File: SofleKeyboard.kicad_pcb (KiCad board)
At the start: 2 copper layers, 82 parts, among them J3 OLED, SW1 SW_PUSH_LED, SW10 SW_PUSH_LED, SW11 SW_PUSH_LED, SW12 SW_PUSH_LED, SW13 SW_PUSH_LED, SW14 SW_PUSH_LED, SW15 SW_PUSH_LED, SW16 SW_PUSH_LED, SW17 SW_PUSH_LED, SW18 SW_PUSH_LED, SW19 SW_PUSH_LED, SW2 SW_PUSH_LED, SW20 SW_PUSH_LED, SW21 SW_PUSH_LED, SW22 SW_PUSH_LED, SW23 SW_PUSH_LED, SW24 SW_PUSH_LED, SW26 SW_PUSH_LED, SW27 SW_PUSH_LED, SW28 SW_PUSH_LED, SW29 SW_PUSH_LED, SW3 SW_PUSH_LED, SW30 SW_PUSH_LED, SW4 SW_PUSH_LED, SW5 SW_PUSH_LED, SW6 SW_PUSH_LED, SW7 SW_PUSH_LED, SW8 SW_PUSH_LED, SW9 SW_PUSH_LED, U1 ProMicro

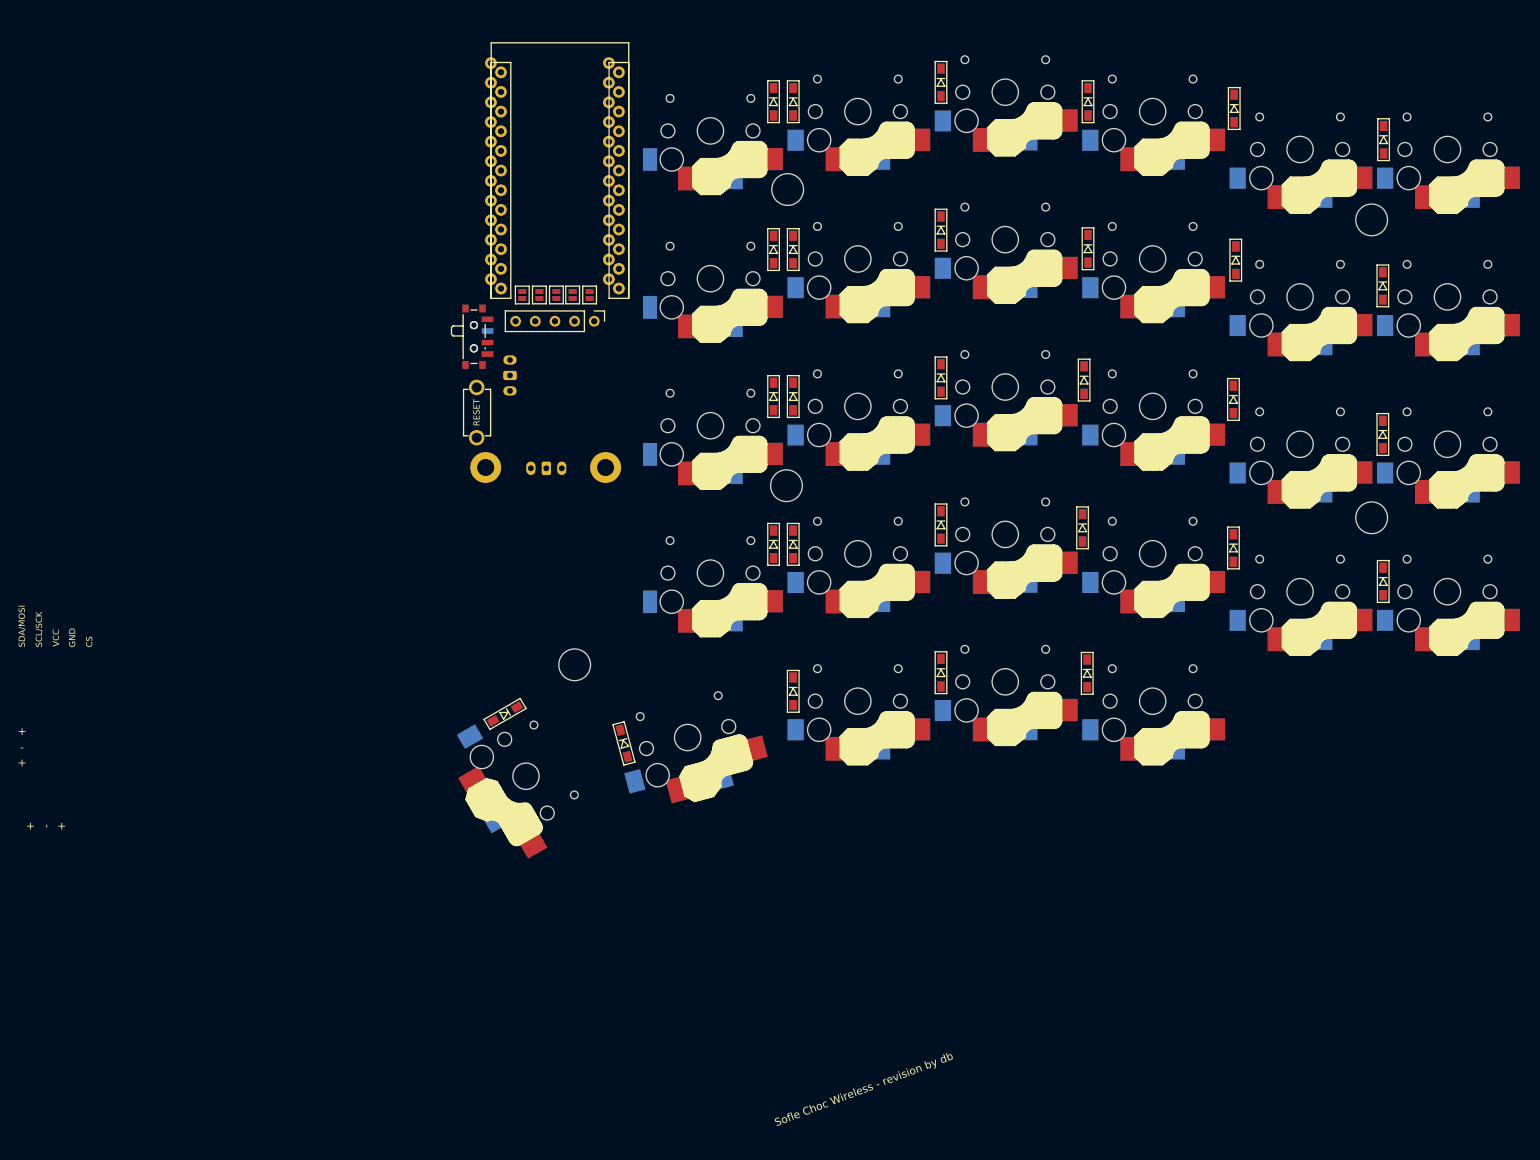
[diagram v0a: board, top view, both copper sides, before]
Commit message: add sofle library, pcb outline, link new footprints to pcb
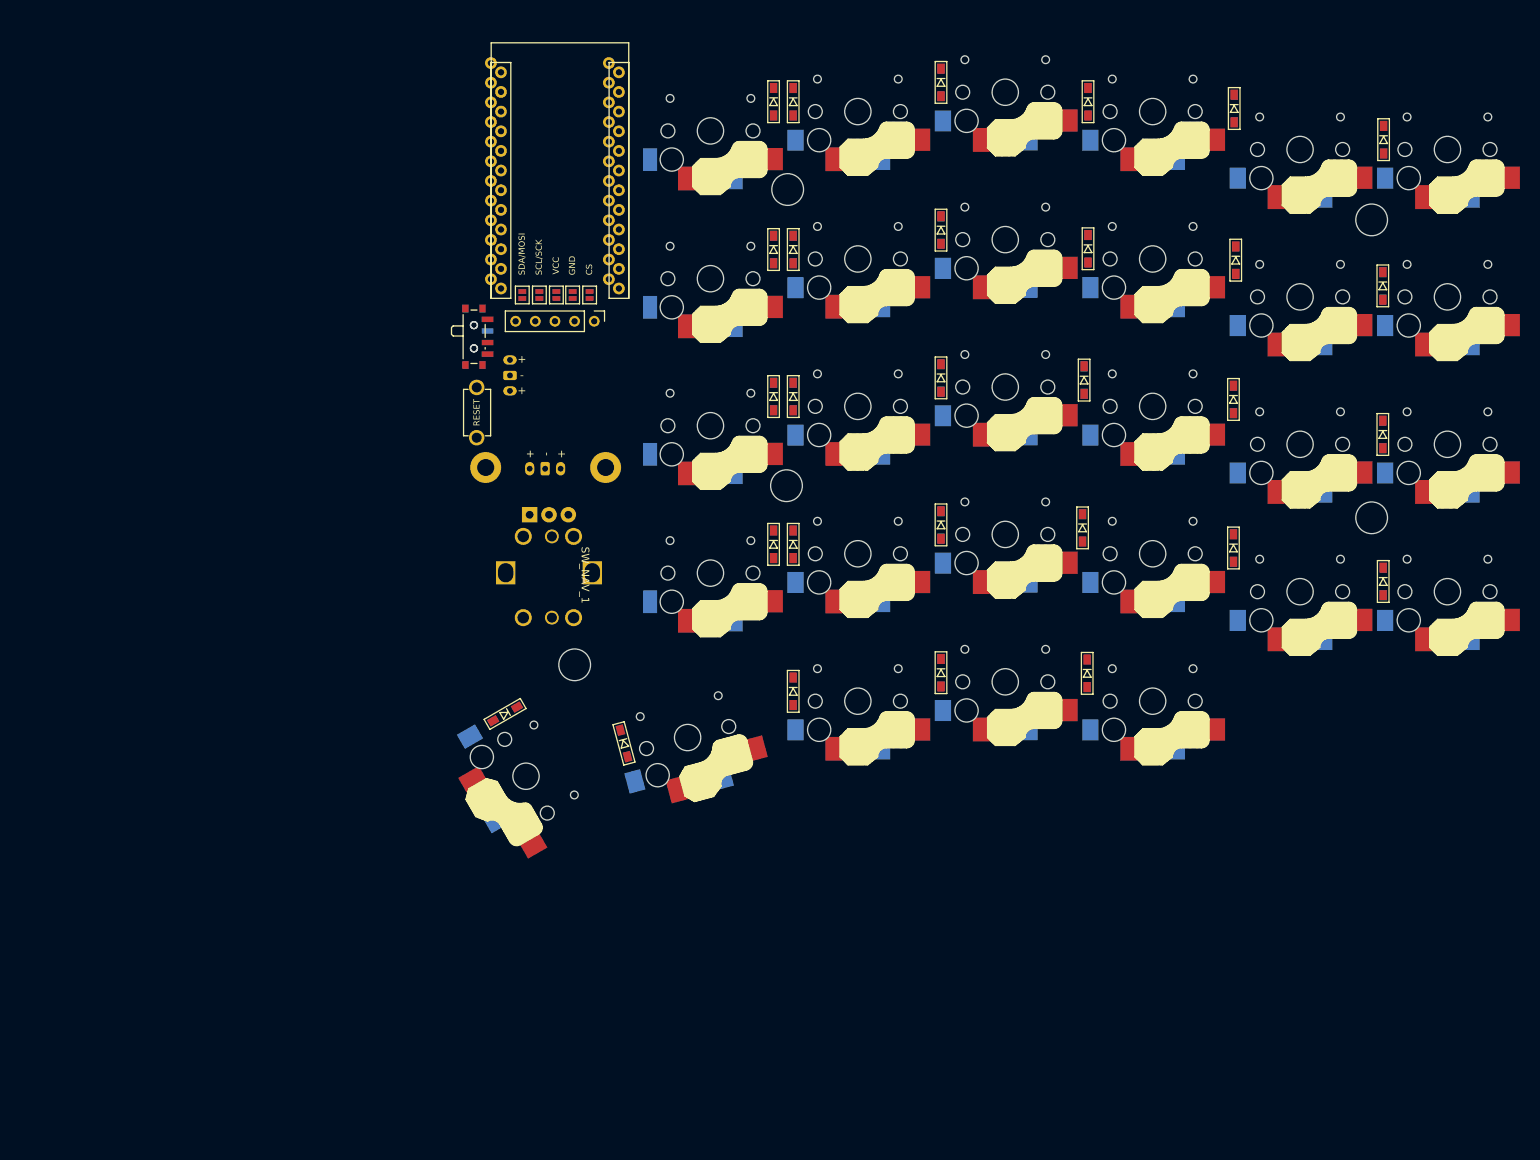
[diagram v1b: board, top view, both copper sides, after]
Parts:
- added ENC1: RotaryEncoder, Rotary_Encoder:RotaryEncoder_Alps_EC12E_Vertical_H20mm, B.Cu at (161.8, 51.6)
- added SW_NAV_1: SW_NAV, VicoKeyboard:NavSwitch_5Way, F.Cu at (168.5, 59.4)
- moved JST_BATT1 0.16 mm to (163.8, 45.7)
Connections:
- U1 pad 2: LED -> unconnected-(U1-RX(PD2)-Pad2)
- U1 pad 7: unconnected-(U1-Pad7) -> col6
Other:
- board text removed: "Sofle Choc Wireless - revision by db"
- board text removed: "s25"

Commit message: jlc rules, add board outline in edge.cuts
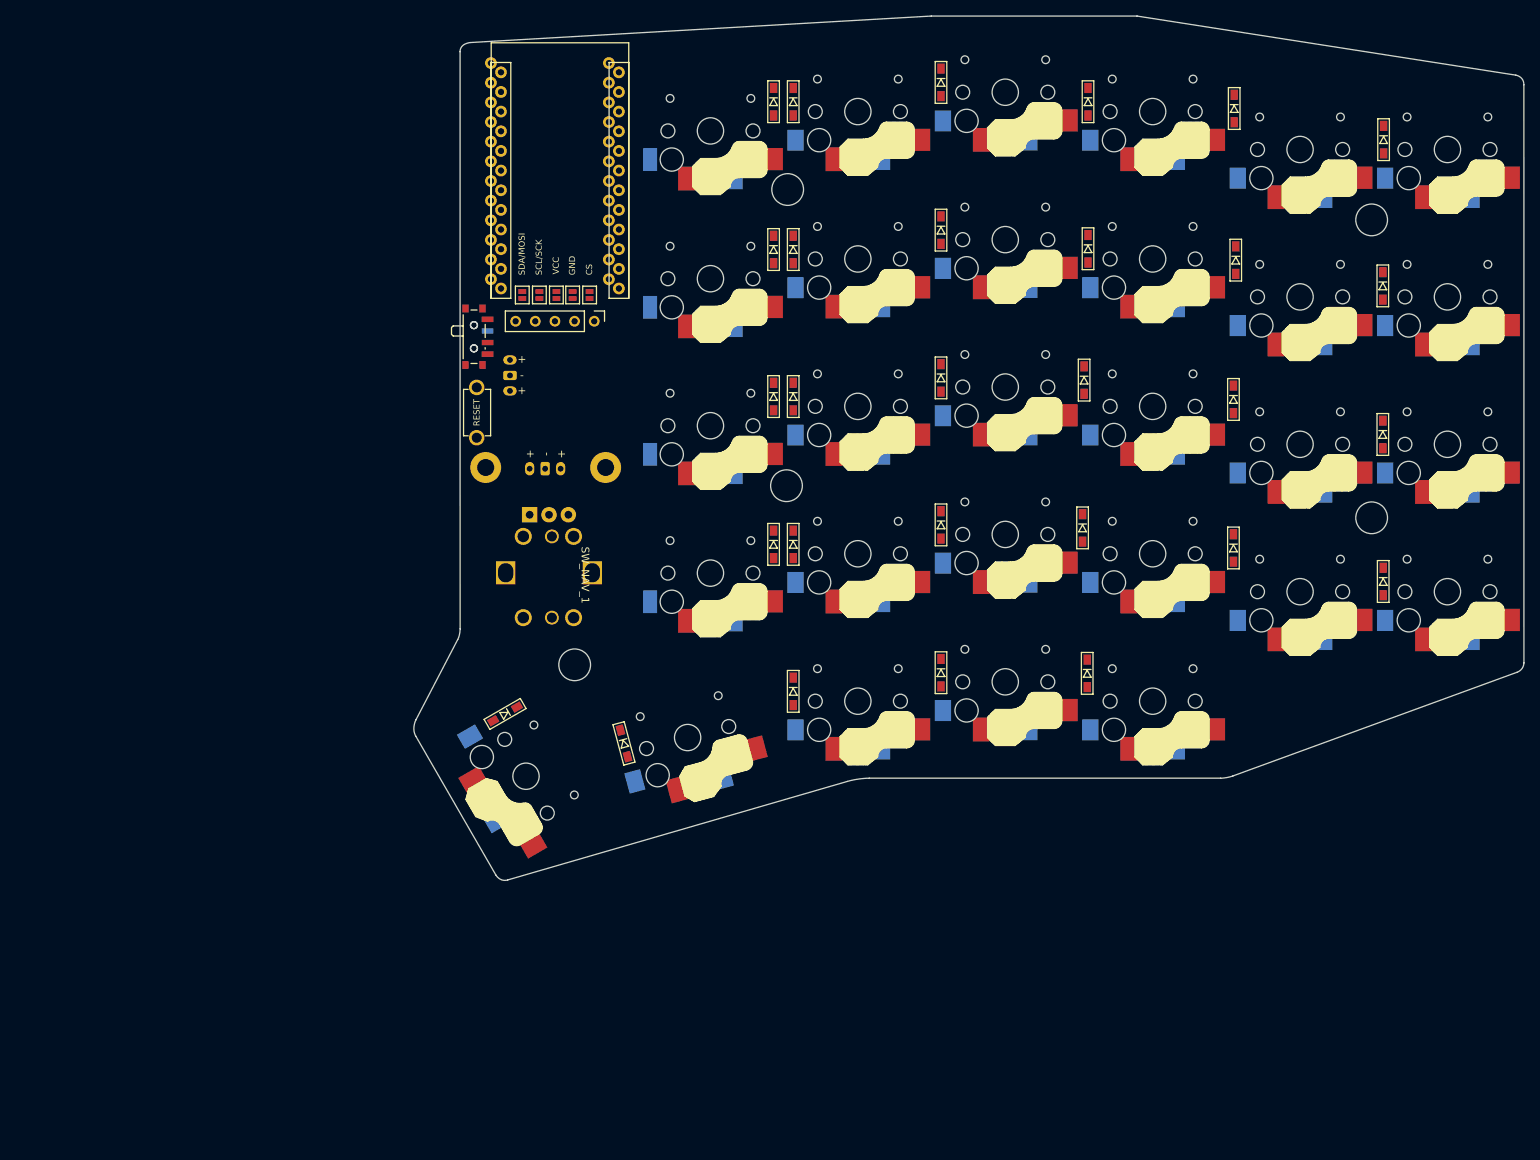
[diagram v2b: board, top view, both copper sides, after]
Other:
- board outline added: 143.5 x 111.7 mm
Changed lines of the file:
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@@
 		(layer "Eco2.User")
+	)
+	(gr_line
+		(start 152.544668 67.678709)
+		(end 147.133363 78.070818)
+		(stroke
+			(width 0.15)
+			(type default)
+		)
+		(layer "Edge.Cuts")
+	)
+	(gr_line
+		(start 213.73912 -12.89736)
+		(end 154.227373 -9.476797)
+		(stroke
+			(width 0.15)
+			(type default)
+		)
+		(layer "Edge.Cuts")
+	)
+	(gr_curve
+		(pts
+			(xy 289.429304 71.917063) (xy 290.339218 71.583746) (xy 290.33912 70.70264) (xy 290.33912 70.70264)
+		)
+		(stroke
+			(width 0.15)
+			(type default)
+		)
+		(layer "Edge.Cuts")
+	)
+	(gr_curve
+		(pts
+			(xy 290.330809 -4.020579) (xy 290.330809 -5.09736) (xy 289.288833 -5.259935) (xy 289.288833 -5.259935)
+		)
+		(stroke
+			(width 0.15)
+			(type default)
+		)
+		(layer "Edge.Cuts")
+	)
+	(gr_line
+		(start 159.003492 98.751015)
+		(end 202.900441 86.016831)
+		(stroke
+			(width 0.15)
+			(type default)
+		)
+		(layer "Edge.Cuts")
+	)
+	(gr_line
+		(start 252.72346 85.313033)
+		(end 289.429304 71.917063)
+		(stroke
+			(width 0.15)
+			(type default)
+		)
+		(layer "Edge.Cuts")
+	)
+	(gr_curve
+		(pts
+			(xy 290.33912 70.70264) (xy 290.33912 70.70264) (xy 290.33912 70.70264) (xy 290.33912 70.70264)
+		)
+		(stroke
+			(width 0.15)
+			(type default)
+		)
+		(layer "Edge.Cuts")
+	)
+	(gr_line
+		(start 290.33912 70.70264)
+		(end 290.330809 -4.020579)
+		(stroke
+			(width 0.15)
+			(type default)
+		)
+		(layer "Edge.Cuts")
+	)
+	(gr_line
+		(start 205.73912 85.599281)
+		(end 251.13912 85.599281)
+		(stroke
+			(width 0.15)
+			(type default)
+		)
+		(layer "Edge.Cuts")
+	)
+	(gr_curve
+		(pts
+			(xy 152.845356 -8.29736) (xy 152.845253 -9.40183) (xy 154.227373 -9.476797) (xy 154.227373 -9.476797)
+		)
+		(stroke
+			(width 0.15)
+			(type default)
+		)
+		(layer "Edge.Cuts")
+	)
+	(gr_curve
+		(pts
+			(xy 152.544668 67.678709) (xy 152.852385 67.087756) (xy 152.852313 66.30264) (xy 152.852313 66.30264)
+		)
+		(stroke
+			(width 0.15)
+			(type default)
+		)
+		(layer "Edge.Cuts")
+	)
+	(gr_line
+		(start 152.845356 -8.29736)
+		(end 152.852313 66.30264)
+		(stroke
+			(width 0.15)
+			(type default)
+		)
+		(layer "Edge.Cuts")
+	)
+	(gr_line
+		(start 147.123018 80.168295)
+		(end 157.474011 98.116267)
+		(stroke
+			(width 0.15)
+			(type default)
+		)
+		(layer "Edge.Cuts")
+	)
+	(gr_curve
+		(pts
+			(xy 251.13912 85.599281) (xy 251.939122 85.599281) (xy 252.72346 85.313033) (xy 252.72346 85.313033)
+		)
+		(stroke
+			(width 0.15)
+			(type default)
+		)
+		(layer "Edge.Cuts")
+	)
+	(gr_line
+		(start 289.288833 -5.259935)
+		(end 240.33912 -12.89736)
+		(stroke
+			(width 0.15)
+			(type default)
+		)
+		(layer "Edge.Cuts")
+	)
+	(gr_line
+		(start 240.33912 -12.89736)
+		(end 213.73912 -12.89736)
+		(stroke
+			(width 0.15)
+			(type default)
+		)
+		(layer "Edge.Cuts")
+	)
+	(gr_curve
+		(pts
+			(xy 202.900441 86.016831) (xy 204.339809 85.599281) (xy 205.73912 85.599281) (xy 205.73912 85.599281)
+		)
+		(stroke
+			(width 0.15)
+			(type default)
+		)
+		(layer "Edge.Cuts")
+	)
+	(gr_curve
+		(pts
+			(xy 147.123018 80.168295) (xy 146.554492 79.182507) (xy 147.133363 78.070818) (xy 147.133363 78.070818)
+		)
+		(stroke
+			(width 0.15)
+			(type default)
+		)
+		(layer "Edge.Cuts")
+	)
+	(gr_curve
+		(pts
+			(xy 159.003492 98.751015) (xy 158.006829 99.04014) (xy 157.474011 98.116267) (xy 157.474011 98.116267)
+		)
+		(stroke
+			(width 0.15)
+			(type default)
+		)
+		(layer "Edge.Cuts")
+	)
+	(gr_curve
+		(pts
+			(xy 205.73912 85.599281) (xy 205.73912 85.599281) (xy 205.73912 85.599281) (xy 205.73912 85.599281)
+		)
+		(stroke
+			(width 0.15)
+			(type default)
+		)
+		(layer "Edge.Cuts")
 	)
 	(gr_text "+"
